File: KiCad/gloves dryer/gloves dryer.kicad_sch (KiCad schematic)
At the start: 7 parts, among them Q1 PN2222A, Q2 PN2222A, U1 PIC16F18126-I/P

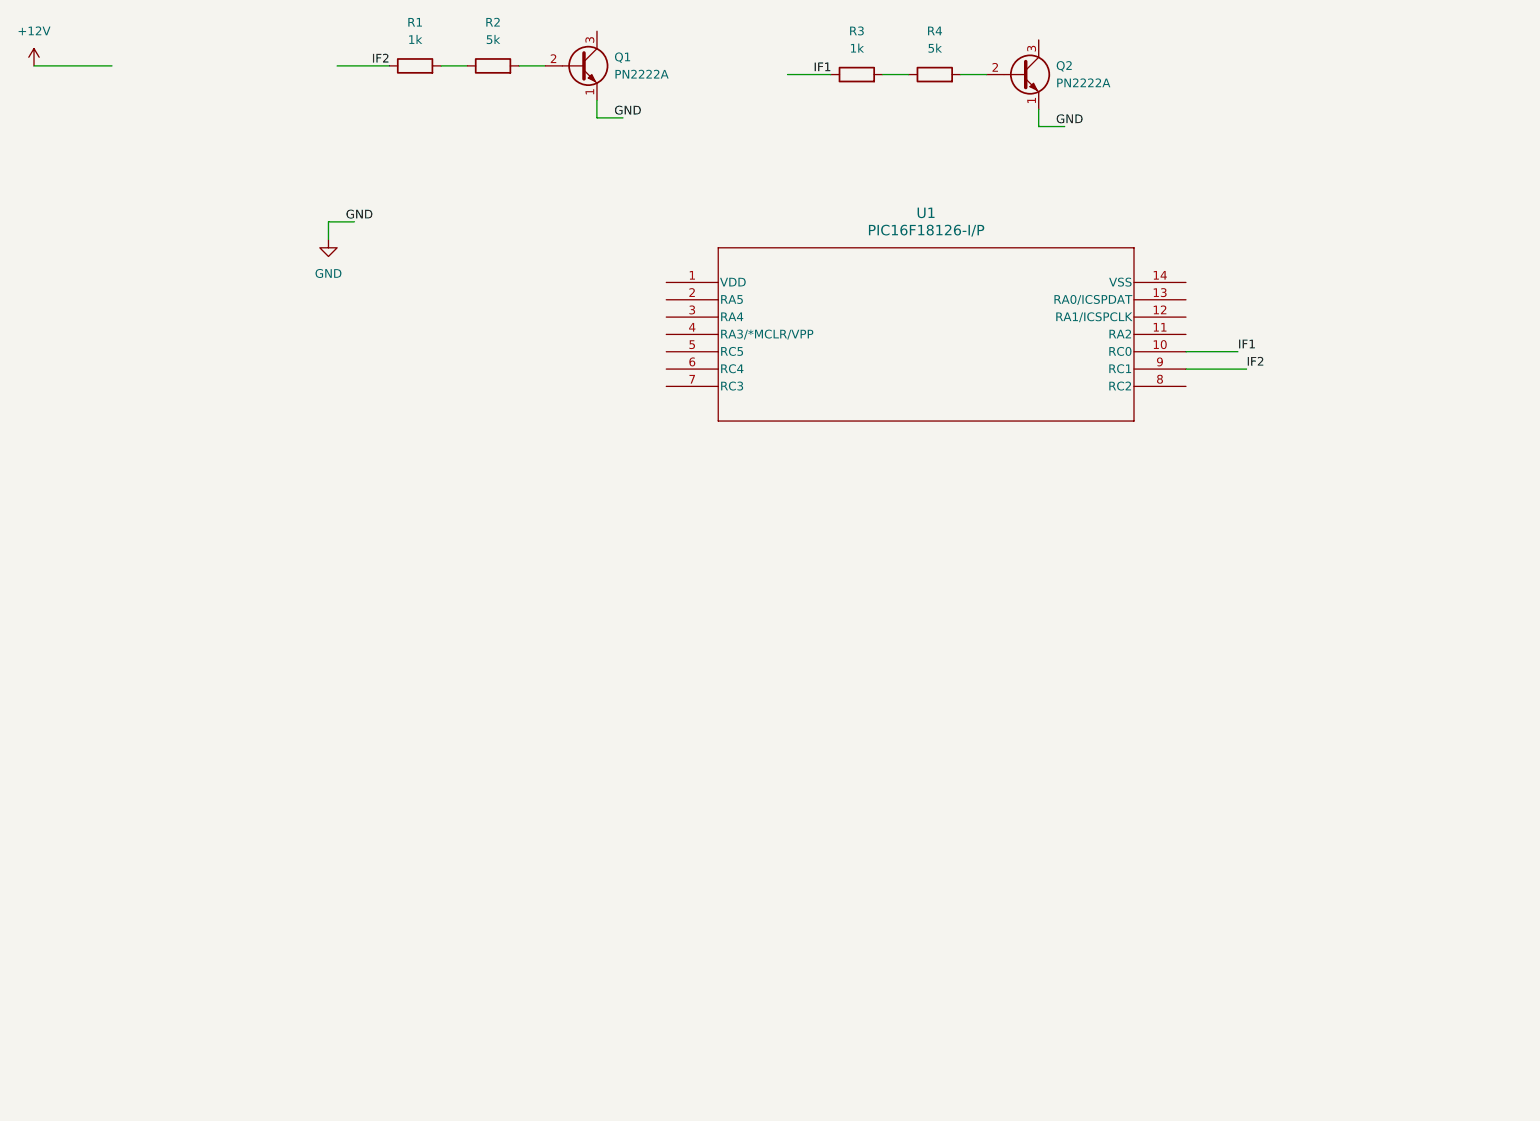
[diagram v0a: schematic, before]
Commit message: Finish V2 schematic with added button and first PCB layout, tolarance have to be double check before sending for manufacturing
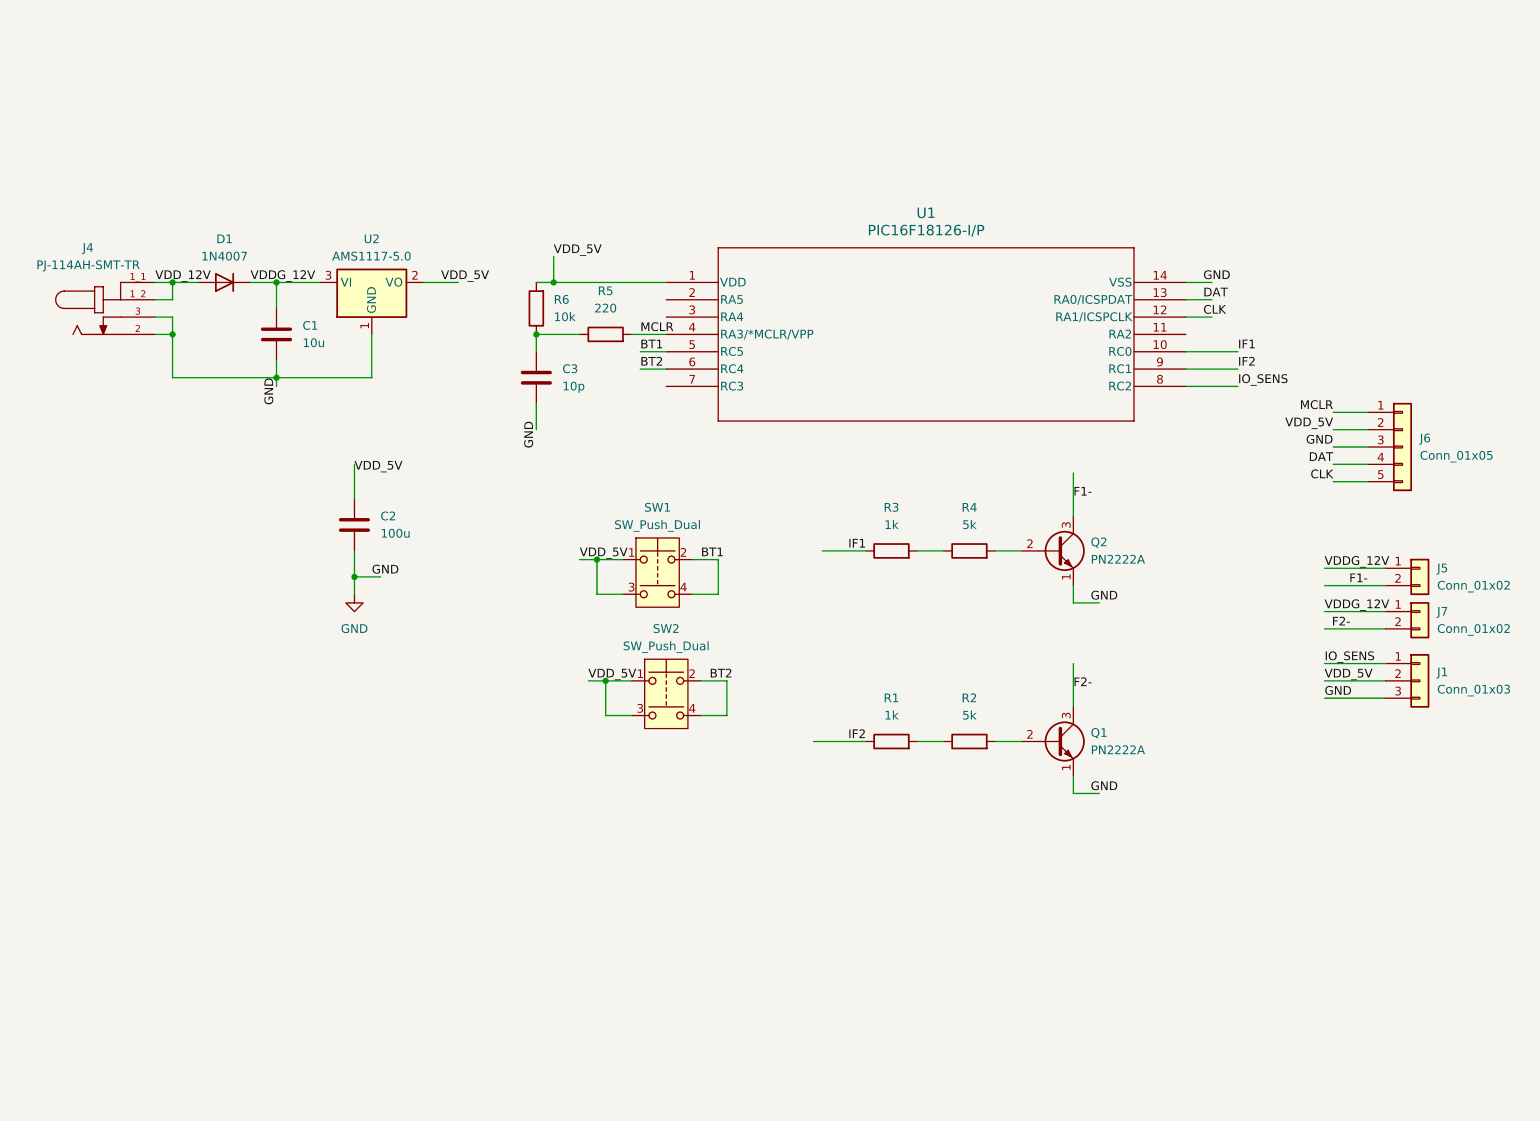
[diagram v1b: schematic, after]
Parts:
- added C1: 10u, Capacitor_THT:C_Radial_D5.0mm_H11.0mm_P2.00mm, symbol Device:C
- added C2: 100u, Capacitor_THT:C_Radial_D6.3mm_H11.0mm_P2.50mm, symbol Device:C
- added C3: 10p, Capacitor_THT:C_Disc_D3.0mm_W1.6mm_P2.50mm, symbol Device:C
- added D1: 1N4007, Diode_THT:D_DO-41_SOD81_P10.16mm_Horizontal, symbol Diode:1N4007
- added J1: Conn_01x03, Connector_PinHeader_2.00mm:PinHeader_1x03_P2.00mm_Vertical, symbol Connector_Generic:Conn_01x03
- added J4: PJ-114AH-SMT-TR, SAMESKY_PJ-114AH-SMT-TR:SAMESKY_PJ-114AH-SMT-TR, symbol SAMESKY_PJ-114AH-SMT-TR:PJ-114AH-SMT-TR
- added J5, J7: Conn_01x02, Connector_PinHeader_2.00mm:PinHeader_2x01_P2.00mm_Vertical, symbol Connector_Generic:Conn_01x02
- added J6: Conn_01x05, Connector_PinHeader_2.00mm:PinHeader_1x05_P2.00mm_Vertical, symbol Connector_Generic:Conn_01x05
- added R5: 220, Resistor_THT:R_Axial_DIN0204_L3.6mm_D1.6mm_P7.62mm_Horizontal, symbol Device:R
- added R6: 10k, Resistor_THT:R_Axial_DIN0204_L3.6mm_D1.6mm_P7.62mm_Horizontal, symbol Device:R
- added SW1, SW2: SW_Push_Dual, Button_Switch_THT:SW_PUSH_6mm_H5mm, symbol Switch:SW_Push_Dual
- added U2: AMS1117-5.0, Package_TO_SOT_SMD:SOT-223-3_TabPin2, symbol Regulator_Linear:AMS1117-5.0
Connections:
- net GND: now also U1.14 (VSS), C1.2, C2.2, C3.2, J1.3 (Pin_3), J4.2, J4.3, J6.3 (Pin_3), U2.1 (GND)
- net VDD_5V: now reaches U1.1 (VDD)
- net VDD_5V: now also C2.1, J1.2 (Pin_2), J6.2 (Pin_2), R6.2, SW1.1, SW1.3, SW2.1, SW2.3, U2.2 (VO)
- net CLK: now reaches U1.12 (RA1/ICSPCLK)
- net CLK: now also J6.5 (Pin_5)
- net DAT: now reaches U1.13 (RA0/ICSPDAT)
- net DAT: now also J6.4 (Pin_4)
- net MCLR: now reaches U1.4 (RA3/*MCLR/VPP)
- net MCLR: now also J6.1 (Pin_1), R5.2
- net BT1: now reaches U1.5 (RC5)
- net BT1: now also SW1.2, SW1.4
- net BT2: now reaches U1.6 (RC4)
- net BT2: now also SW2.2, SW2.4
- net IO_SENS: now reaches U1.8 (RC2)
- net IO_SENS: now also J1.1 (Pin_1)
- net F1-: now reaches Q2.3 (C)
- net F1-: now also J5.2 (Pin_2)
- net F2-: now reaches Q1.3 (C)
- net F2-: now also J7.2 (Pin_2)
- new net: C3.1, R5.1, R6.1
- new net VDDG_12V: C1.1, D1.1 (K), J5.1 (Pin_1), J7.1 (Pin_1), U2.3 (VI)
- new net VDD_12V: D1.2 (A), J4.1_1, J4.1_2
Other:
- moved on the sheet: Q1, Q2, R1, R2, R3, R4

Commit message: Finished PCB, working on firmware for added switch state
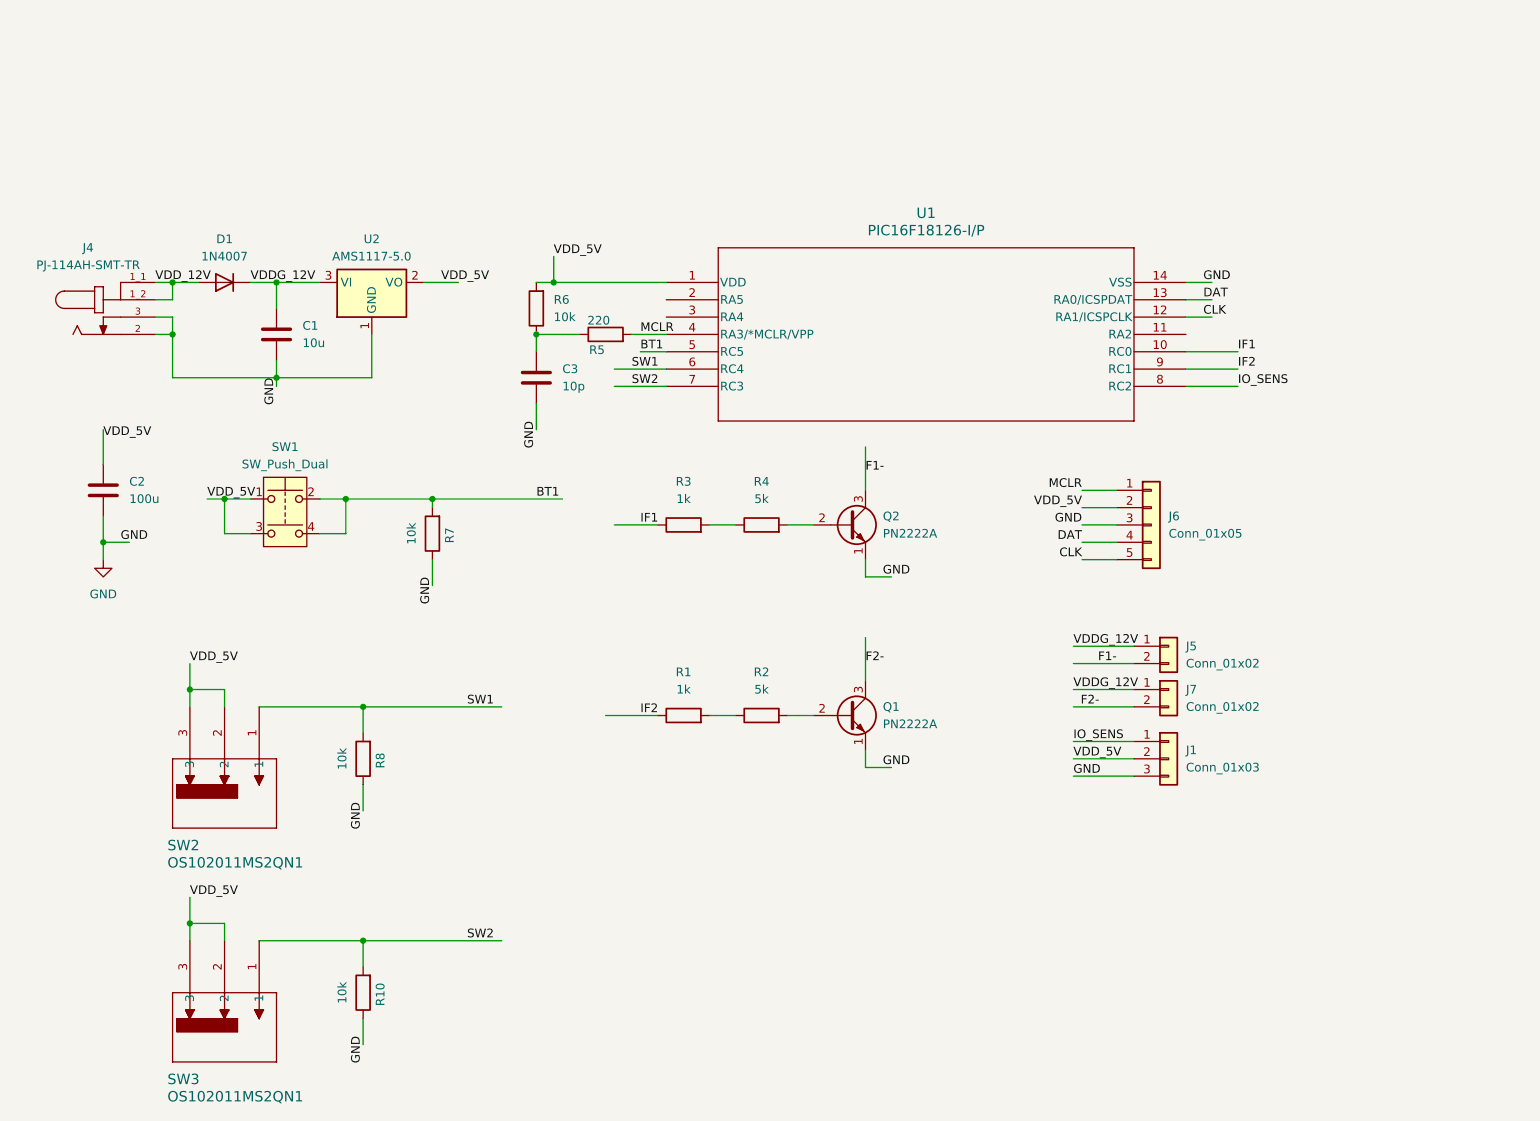
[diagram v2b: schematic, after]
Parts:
- removed SW2: SW_Push_Dual, Button_Switch_THT:SW_PUSH_6mm_H5mm, symbol Switch:SW_Push_Dual
- added R10, R7, R8: 10k, Resistor_THT:R_Axial_DIN0204_L3.6mm_D1.6mm_P7.62mm_Horizontal, symbol Device:R
- added SW2, SW3: OS102011MS2QN1, SPDT_OS102011_CNK, symbol OS102011MS2QN1:OS102011MS2QN1
- C1: footprint Capacitor_THT:C_Radial_D5.0mm_H11.0mm_P2.00mm -> Capacitor_THT:CP_Radial_D5.0mm_P2.00mm
- C2: footprint Capacitor_THT:C_Radial_D6.3mm_H11.0mm_P2.50mm -> Capacitor_THT:CP_Radial_D6.3mm_P2.50mm
- Q1, Q2: footprint Package_TO_SOT_THT:TO-92_Inline -> Package_TO_SOT_THT:TO-92_Inline_Wide
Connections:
- net BT1: now also R7.2
- net GND: now also R10.1, R7.1, R8.1
- net VDD_5V: now also SW2.2, SW2.3, SW3.2, SW3.3
- net SW2: now reaches U1.7 (RC3)
- net SW2: now also R10.2, SW3.1
- net BT2 renamed SW1
- net SW1: now also R8.2, SW2.1
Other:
- moved on the sheet: C2, J1, J5, J6, J7, Q1, Q2, R1, R2, R3, R4, SW1
